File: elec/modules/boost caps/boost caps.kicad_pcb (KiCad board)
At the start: 2 copper layers, 40.6 x 61 mm, 8 parts, among them J1 Conn_01x05, J2 Conn_01x05

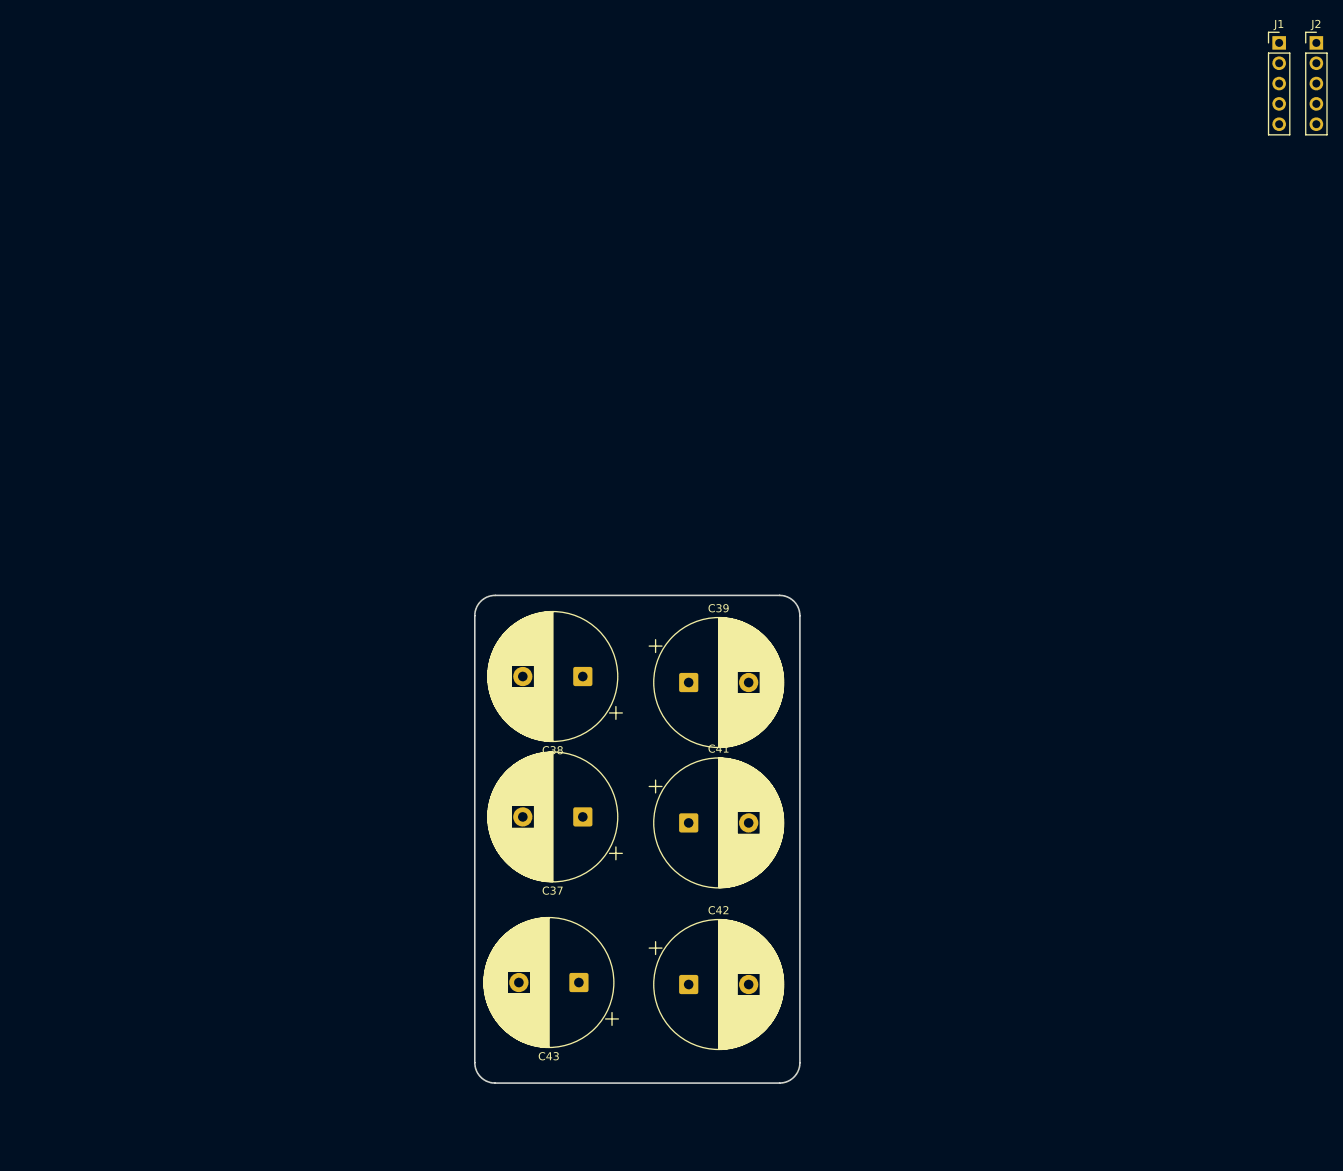
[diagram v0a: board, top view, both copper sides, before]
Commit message: finishe dcaps for boost
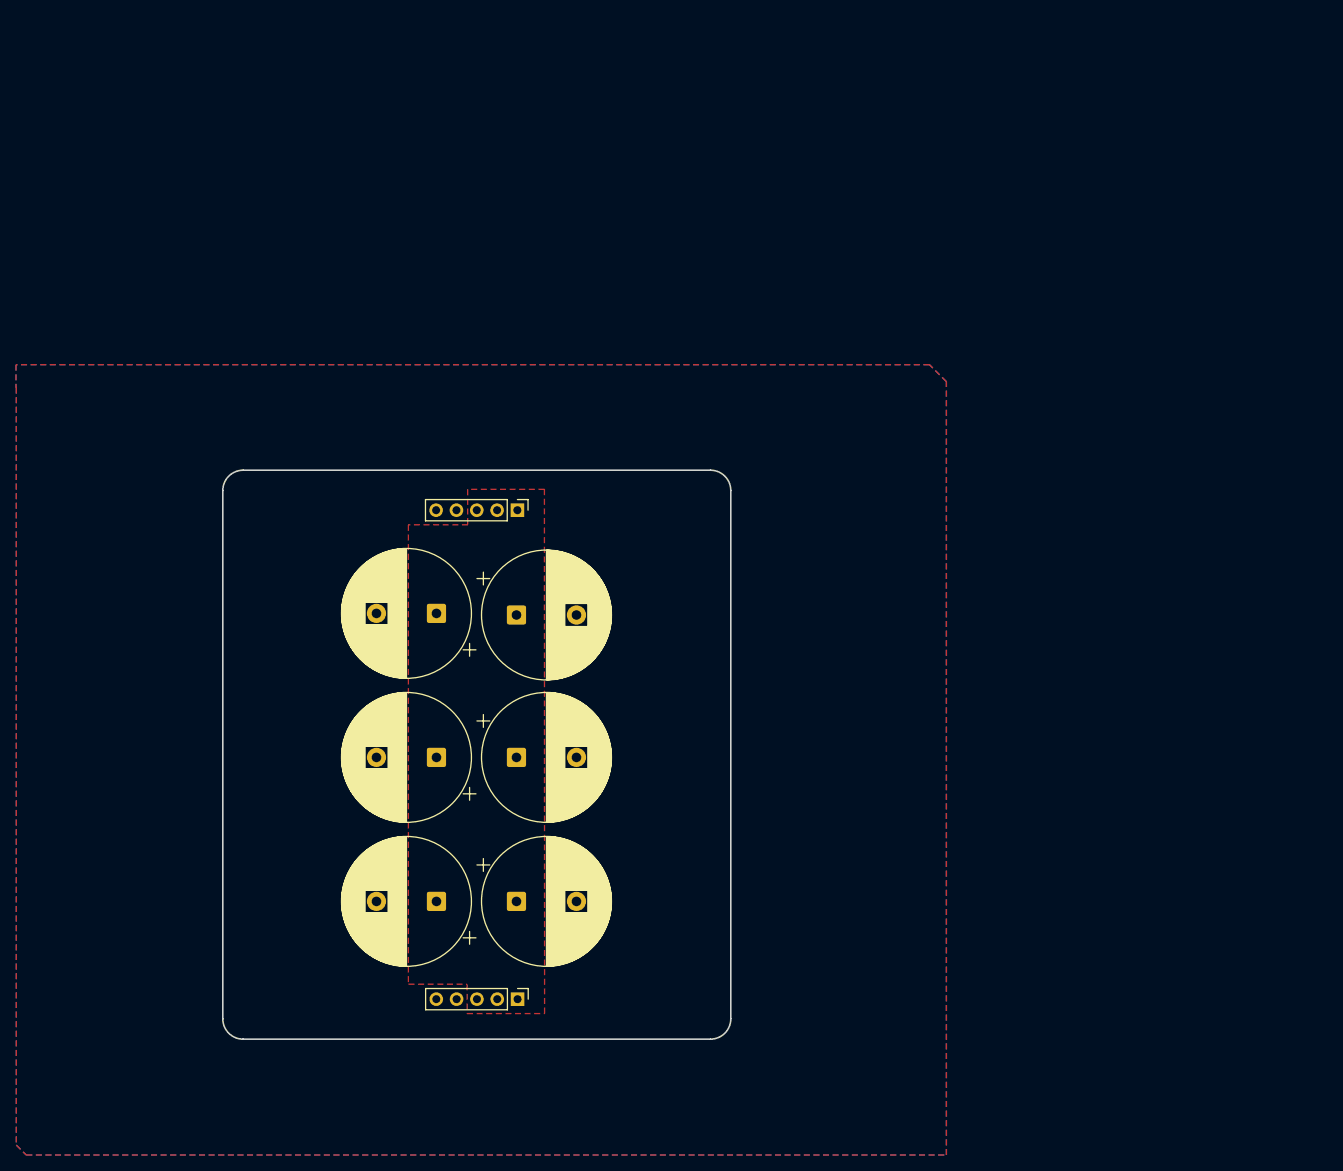
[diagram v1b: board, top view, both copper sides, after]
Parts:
- moved J2 155.7 mm to (127.3, 121.3), turned to -90 degrees
- moved J1 111.7 mm to (127.3, 60.2), turned to -90 degrees
- moved C39 41.7 mm to (117.2, 109.1), turned to 180 degrees
- moved C42 35.6 mm to (127.2, 91.1)
- moved C41 33.7 mm to (127.2, 73.3)
- moved C37 31.3 mm to (117.2, 73.1)
- moved C38 20.9 mm to (117.2, 91.1)
- moved C43 12.8 mm to (127.2, 109.1), turned to 0 degrees
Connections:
- net +12V renamed +24V
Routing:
- added copper zone on F.Cu, net +24V
- added copper zone on B.Cu, net GND
- added copper zone on F.Cu, net GND
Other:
- board size 40.6 x 61 mm -> 63.5 x 71.1 mm

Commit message: added silkscreen
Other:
- board text added: "design of 2-Chairs. 2025 JLC Order No. JLCJLCJLCJLC"
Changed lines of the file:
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@@
 		(layer "Edge.Cuts")
+	)
+	(gr_text "design of 2-Chairs. 2025\nJLC Order No. JLCJLCJLCJLC"
+		(at 122.25 99.269999 0)
+		(layer "B.SilkS")
+		(effects
+			(font
+				(size 1 1)
+				(thickness 0.2)
+			)
+			(justify mirror)
+		)
 	)
 	(zone

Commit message: added name cos why not
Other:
- board text added: "Design By Euston Tan"
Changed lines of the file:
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@@
 		(layer "Edge.Cuts")
+	)
+	(gr_text "Design By Euston Tan \n"
+		(at 122.25 124.769999 0)
+		(layer "B.SilkS")
+		(effects
+			(font
+				(size 1 1)
+				(thickness 0.2)
+				(bold yes)
+			)
+			(justify mirror)
+		)
 	)
 	(gr_text "design of 2-Chairs. 2025\nJLC Order No. JLCJLCJLCJLC"

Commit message: chore: boostcaps production files
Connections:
- J1 pad 3: +24V -> unconnected-(J1-Pin_3-Pad3)
- J1 pad 4: unconnected-(J1-Pin_4-Pad4) -> GND
- J2 pad 3: +24V -> unconnected-(J2-Pin_3-Pad3)
- J2 pad 4: unconnected-(J2-Pin_4-Pad4) -> GND
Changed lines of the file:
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@@
 	(net 0 "")
 	(net 1 "GND")
-	(net 2 "unconnected-(J1-Pin_4-Pad4)")
-	(net 3 "unconnected-(J2-Pin_4-Pad4)")
+	(net 2 "unconnected-(J1-Pin_3-Pad3)")
+	(net 3 "unconnected-(J2-Pin_3-Pad3)")
 	(net 4 "+24V")
 	(footprint "Capacitor_THT:CP_Radial_D16.0mm_P7.50mm"
@@
 		(sheetname "/")
 		(sheetfile "boost caps.kicad_sch")
-		(attr through_hole)
+		(attr through_hole exclude_from_pos_files exclude_from_bom)
 		(fp_line
 			(start 11.83 -0.765)
@@
 		(sheetname "/")
 		(sheetfile "boost caps.kicad_sch")
-		(attr through_hole)
+		(attr through_hole exclude_from_pos_files exclude_from_bom)
 		(fp_line
 			(start -4.939491 -4.555)
@@
 		(sheetname "/")
 		(sheetfile "boost caps.kicad_sch")
-		(attr through_hole)
+		(attr through_hole exclude_from_pos_files exclude_from_bom)
 		(fp_line
 			(start 11.83 -0.765)
@@
 		(sheetname "/")
 		(sheetfile "boost caps.kicad_sch")
-		(attr through_hole)
+		(attr through_hole exclude_from_pos_files exclude_from_bom)
 		(fp_line
 			(start -4.939491 -4.555)
@@
 		(sheetname "/")
 		(sheetfile "boost caps.kicad_sch")
-		(attr through_hole)
+		(attr through_hole exclude_from_pos_files exclude_from_bom)
 		(fp_line
 			(start -1.33 11.49)
@@
 			(layers "*.Cu" "*.Mask")
 			(remove_unused_layers no)
-			(net 4 "+24V")
+			(net 3 "unconnected-(J2-Pin_3-Pad3)")
 			(pinfunction "Pin_3")
-			(pintype "passive")
+			(pintype "passive+no_connect")
 		)
 		(pad "4" thru_hole oval
@@
 			(layers "*.Cu" "*.Mask")
 			(remove_unused_layers no)
-			(net 3 "unconnected-(J2-Pin_4-Pad4)")
+			(net 1 "GND")
 			(pinfunction "Pin_4")
-			(pintype "passive+no_connect")
+			(pintype "passive")
 		)
 		(pad "5" thru_hole oval
@@
 		(sheetname "/")
 		(sheetfile "boost caps.kicad_sch")
-		(attr through_hole)
+		(attr through_hole exclude_from_pos_files exclude_from_bom)
 		(fp_line
 			(start -1.33 11.49)
@@
 			(layers "*.Cu" "*.Mask")
 			(remove_unused_layers no)
-			(net 4 "+24V")
+			(net 2 "unconnected-(J1-Pin_3-Pad3)")
 			(pinfunction "Pin_3")
-			(pintype "passive")
+			(pintype "passive+no_connect")
 		)
 		(pad "4" thru_hole oval
@@
 			(layers "*.Cu" "*.Mask")
 			(remove_unused_layers no)
-			(net 2 "unconnected-(J1-Pin_4-Pad4)")
+			(net 1 "GND")
 			(pinfunction "Pin_4")
-			(pintype "passive+no_connect")
+			(pintype "passive")
 		)
 		(pad "5" thru_hole oval
@@
 		(sheetname "/")
 		(sheetfile "boost caps.kicad_sch")
-		(attr through_hole)
+		(attr through_hole exclude_from_pos_files exclude_from_bom)
 		(fp_line
 			(start -4.939491 -4.555)
@@
 		(sheetname "/")
 		(sheetfile "boost caps.kicad_sch")
-		(attr through_hole)
+		(attr through_hole exclude_from_pos_files exclude_from_bom)
 		(fp_line
 			(start 11.83 -0.765)
@@
 	)
 	(gr_text "Design By Euston Tan \n"
-		(at 122.25 124.769999 0)
+		(at 122.25 99.769999 0)
 		(layer "B.SilkS")
 		(effects
@@
 	)
 	(gr_text "design of 2-Chairs. 2025\nJLC Order No. JLCJLCJLCJLC"
-		(at 122.25 99.269999 0)
+		(at 122.25 81.769999 0)
 		(layer "B.SilkS")
 		(effects
@@
 		(polygon
 			(pts
-				(xy 121.03 123.129999) (xy 130.722754 123.129999) (xy 130.702754 57.599999) (xy 121.11 57.599999)
-				(xy 121.11 61.999999) (xy 121.14 62.029999) (xy 113.717245 62.029999) (xy 113.697245 62.049999)
-				(xy 113.697245 119.439999) (xy 113.717245 119.459999) (xy 121.02 119.459999) (xy 121.03 119.469999)
+				(xy 123.775835 123.103704) (xy 130.722754 123.129999) (xy 130.702754 57.599999) (xy 123.51 57.599999)
+				(xy 123.51 62.019999) (xy 113.717245 62.029999) (xy 113.697245 62.049999) (xy 113.697245 119.439999)
+				(xy 113.717245 119.459999) (xy 123.75 119.459999)
 			)
 		)

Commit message: fix: boostcaps revision number; chore: boostcaps production files
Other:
- board text added: "design of 2-Chairs. 2025 JLC Order No. JLCJLCJLCJLC rev. 1.0"
- board text removed: "design of 2-Chairs. 2025 JLC Order No. JLCJLCJLCJLC"
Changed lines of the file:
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@@
 		)
 	)
-	(gr_text "design of 2-Chairs. 2025\nJLC Order No. JLCJLCJLCJLC"
+	(gr_text "design of 2-Chairs. 2025\nJLC Order No. JLCJLCJLCJLC\nrev. 1.0"
 		(at 122.25 81.769999 0)
 		(layer "B.SilkS")
